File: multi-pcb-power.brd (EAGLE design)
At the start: 72.1 x 32.7 mm, 24 parts, among them Q5 TIP136, T2 BC618, X1 2.52B-ZR, X2 2.52B-ZR, X3 2.52B-ZR, X4 2.54B-ZR

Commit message: Final design for power circuit
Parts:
- R17: value 26k -> 68k
- R6: value 10k -> 20k
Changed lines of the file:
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@@
 <layers>
 <layer number="1" name="Top" color="4" fill="1" visible="yes" active="yes"/>
-<layer number="16" name="Bottom" color="1" fill="1" visible="yes" active="yes"/>
+<layer number="16" name="Bottom" color="1" fill="1" visible="no" active="yes"/>
 <layer number="17" name="Pads" color="2" fill="1" visible="yes" active="yes"/>
 <layer number="18" name="Vias" color="2" fill="1" visible="yes" active="yes"/>
@@
 <attribute name="VALUE" x="73.025" y="16.0655" size="1.778" layer="28" ratio="10" rot="MR90"/>
 </element>
-<element name="R17" library="rcl" library_urn="urn:adsk.eagle:library:334" package="0207/10" package3d_urn="urn:adsk.eagle:package:23491/2" value="26k" x="27.6225" y="18.0975" smashed="yes" rot="R180">
+<element name="R17" library="rcl" library_urn="urn:adsk.eagle:library:334" package="0207/10" package3d_urn="urn:adsk.eagle:package:23491/2" value="68k" x="27.6225" y="18.0975" smashed="yes" rot="R180">
 <attribute name="NAME" x="25.4" y="19.4945" size="1.27" layer="25" ratio="10"/>
 <attribute name="POPULARITY" value="81" x="-13.0175" y="81.5975" size="1.778" layer="27" rot="R180" display="off"/>
@@
 <attribute name="VALUE" x="30.7975" y="13.7033" size="1.27" layer="27" ratio="10" rot="R180"/>
 </element>
-<element name="R6" library="rcl" library_urn="urn:adsk.eagle:library:334" package="0207/7" package3d_urn="urn:adsk.eagle:package:23493/2" value="10k" x="47.9425" y="14.9225" smashed="yes" rot="R90">
+<element name="R6" library="rcl" library_urn="urn:adsk.eagle:library:334" package="0207/7" package3d_urn="urn:adsk.eagle:package:23493/2" value="20k" x="47.9425" y="14.9225" smashed="yes" rot="R90">
 <attribute name="NAME" x="50.673" y="14.9225" size="1.27" layer="25" ratio="10" rot="R90"/>
 <attribute name="POPULARITY" value="46" x="111.4425" y="45.4025" size="1.778" layer="27" rot="R90" display="off"/>

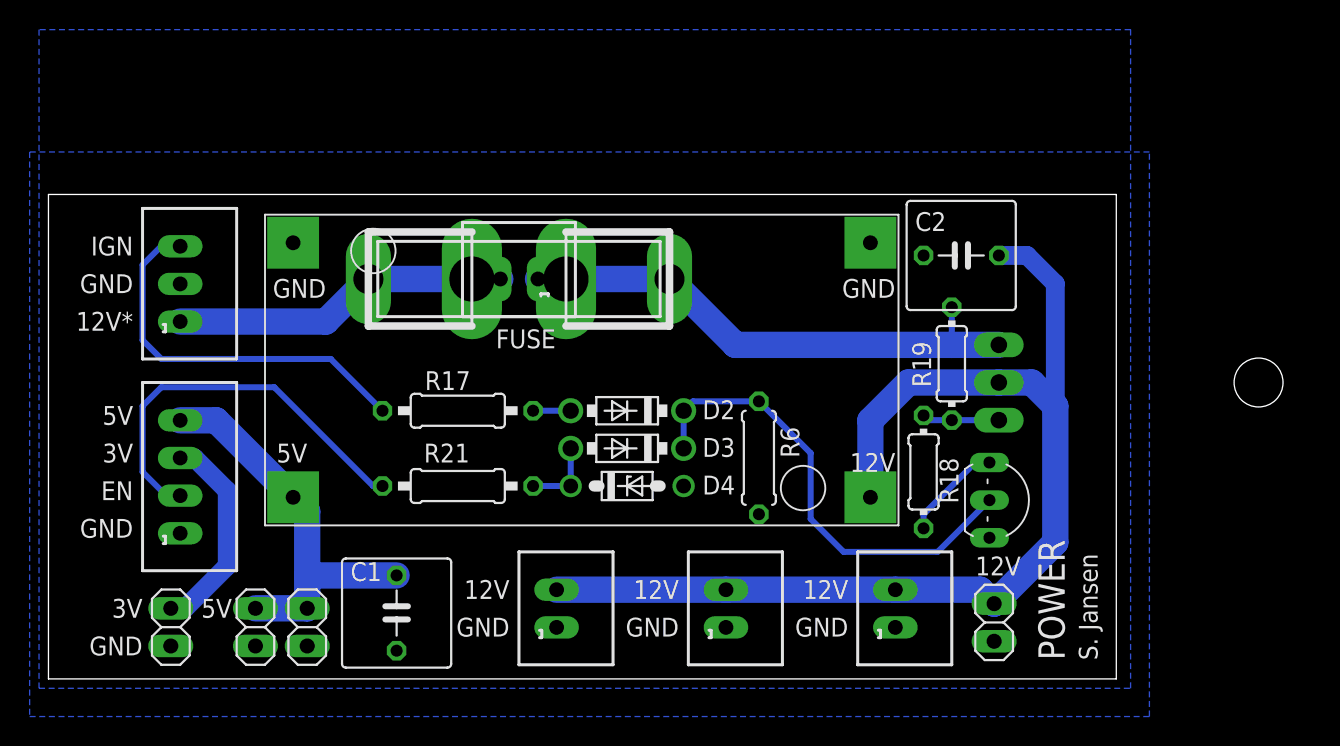
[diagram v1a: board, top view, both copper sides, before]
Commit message: Fixed mosfet direction for power in v3
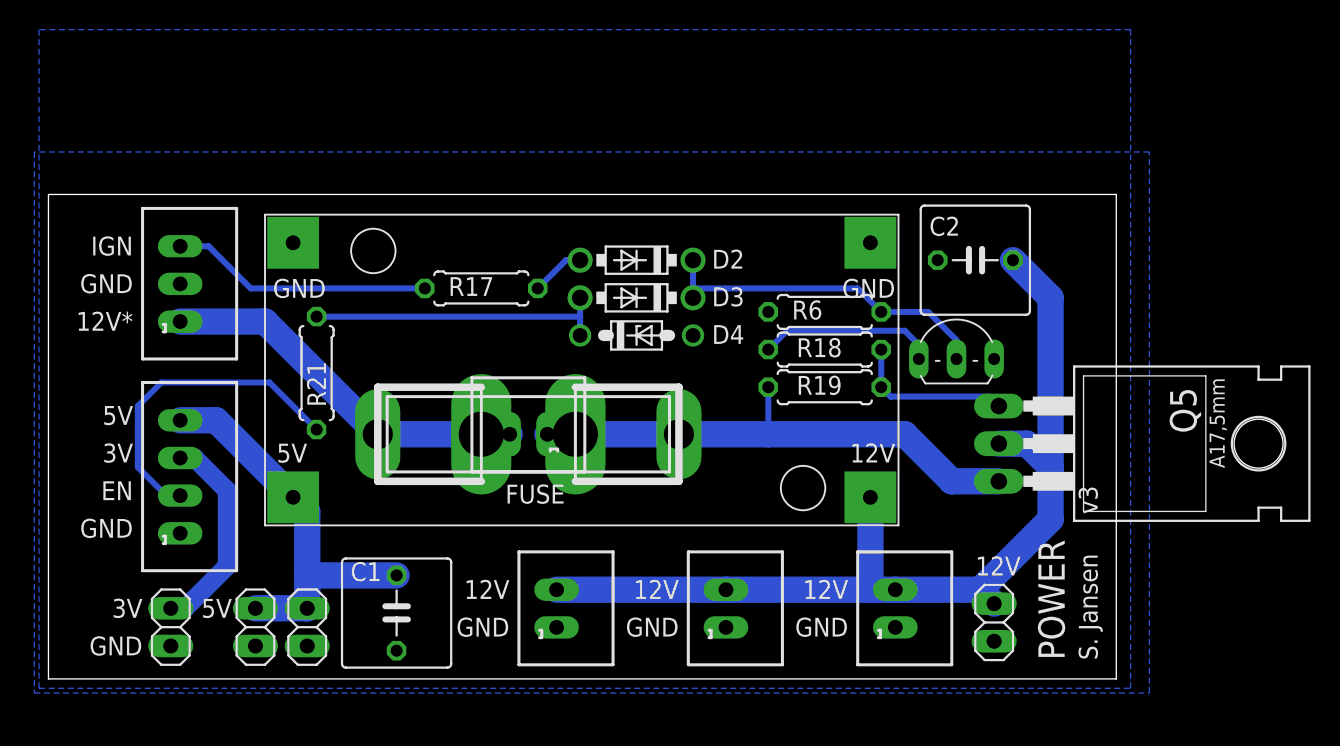
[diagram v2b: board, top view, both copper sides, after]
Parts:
- R17, R21: device rcl:0207/10 -> rcl:0207/7
- R18, R19: device rcl:0204/7 -> rcl:0207/7
- moved R21 12.2 mm to (18.1, 20.6), turned to 270 degrees
- moved T2 11.3 mm to (61.3, 22.9), turned to 0 degrees
- moved R6 10.8 mm to (52.4, 24.8), turned to 0 degrees
- moved R18 10.6 mm to (52.4, 22.2), turned to 180 degrees
- moved FUSE 10.5 mm to (32.4, 16.5)
- moved U$1 10.5 mm to (32.4, 16.5)
- moved D3 10.2 mm to (39.7, 25.7)
- moved D2 10.2 mm to (39.7, 28.3)
- moved D4 10.2 mm to (39.7, 23.2)
- moved R19 8.72 mm to (52.4, 19.7), turned to 180 degrees
- moved R17 8.41 mm to (29.2, 26.4)
- moved Q5 4.13 mm to (70.5, 15.9), flipped to the top, turned to 270 degrees
- moved C2 1.00 mm to (62.5, 28.3)
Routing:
- net N$11: track 5.08 -> 20.3 mm
- net PWR_IN+: track 77.2 -> 65.6 mm
- net N$5: track 31.7 -> 23.0 mm
- net IGNITION: track 26.3 -> 17.7 mm
- net N$14: track 5.21 -> 11.0 mm
- net PWR_ENABLE: track 27.1 -> 21.8 mm
- net N$15: track 6.84 -> 12.0 mm
- net +12V: track 22.8 -> 25.4 mm
- net N$12: track 2.54 -> 4.28 mm
- net N$21: track 35.5 -> 35.0 mm
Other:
- board text added: "v3"
